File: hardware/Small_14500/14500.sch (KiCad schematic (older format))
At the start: 49 parts, among them J2 Battery, J3 GPIO, J4 USB_B_Micro, J5 Power, J6 LEDs, J7 GPIO, Q1 BSS806N, Q2 BSS806N, Q3 BSS806N, Q4 BSS806N, SW1 Mode, SW2 Power, U1 STM32L072KZUx, U2 AP2210N-3.3TRG1, U3 MCP73831T-2ACI_OT, U4 ESD7002WTT1G

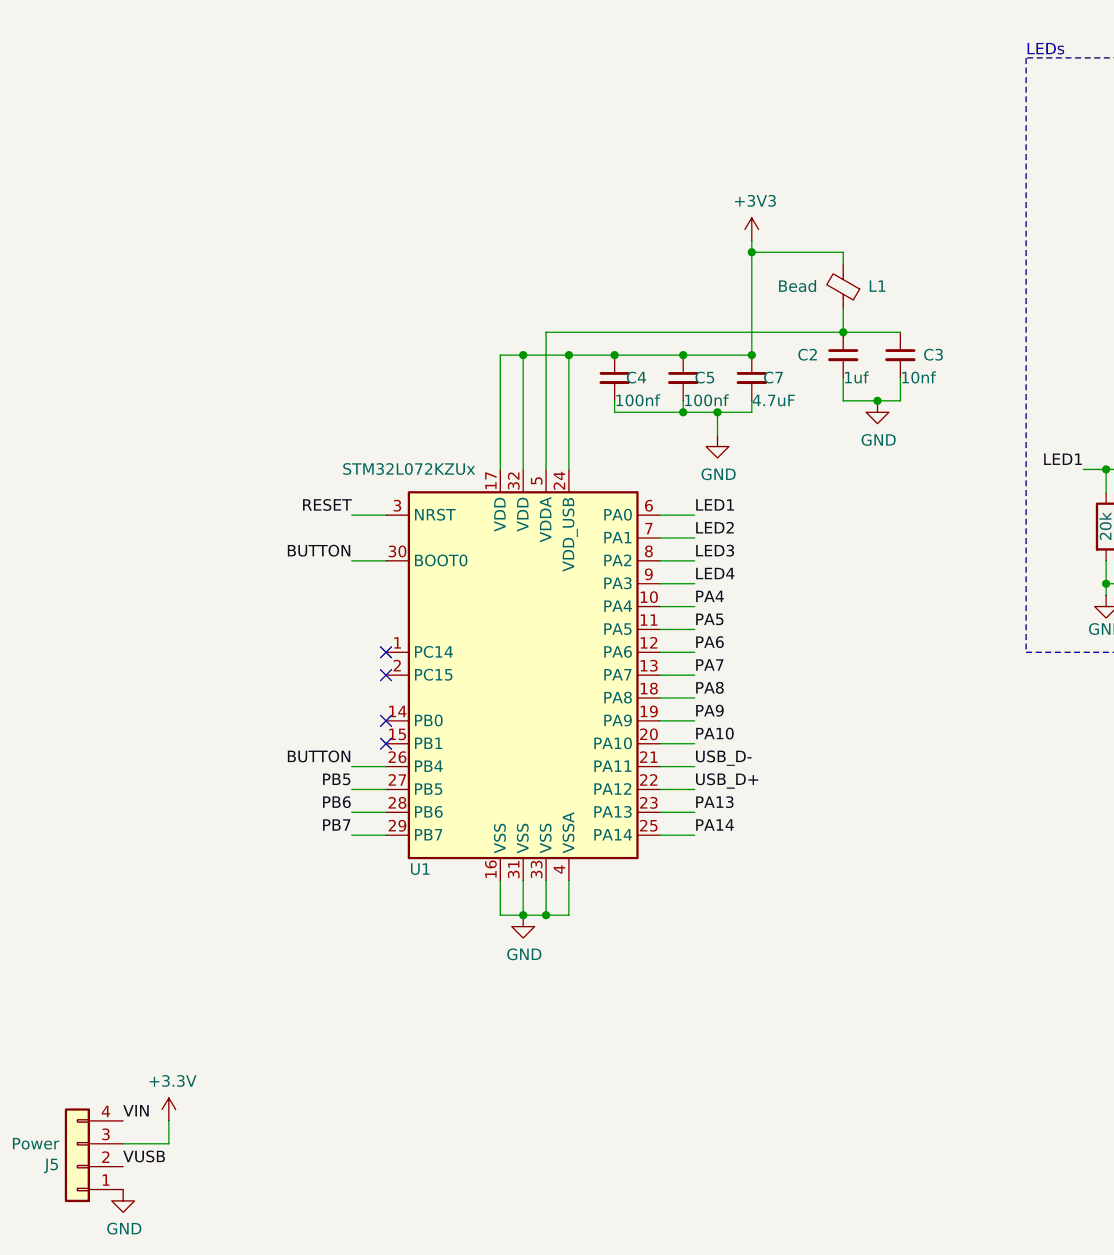
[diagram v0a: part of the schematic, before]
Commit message: Use STM32F412CGUx (Regular & Tiny)
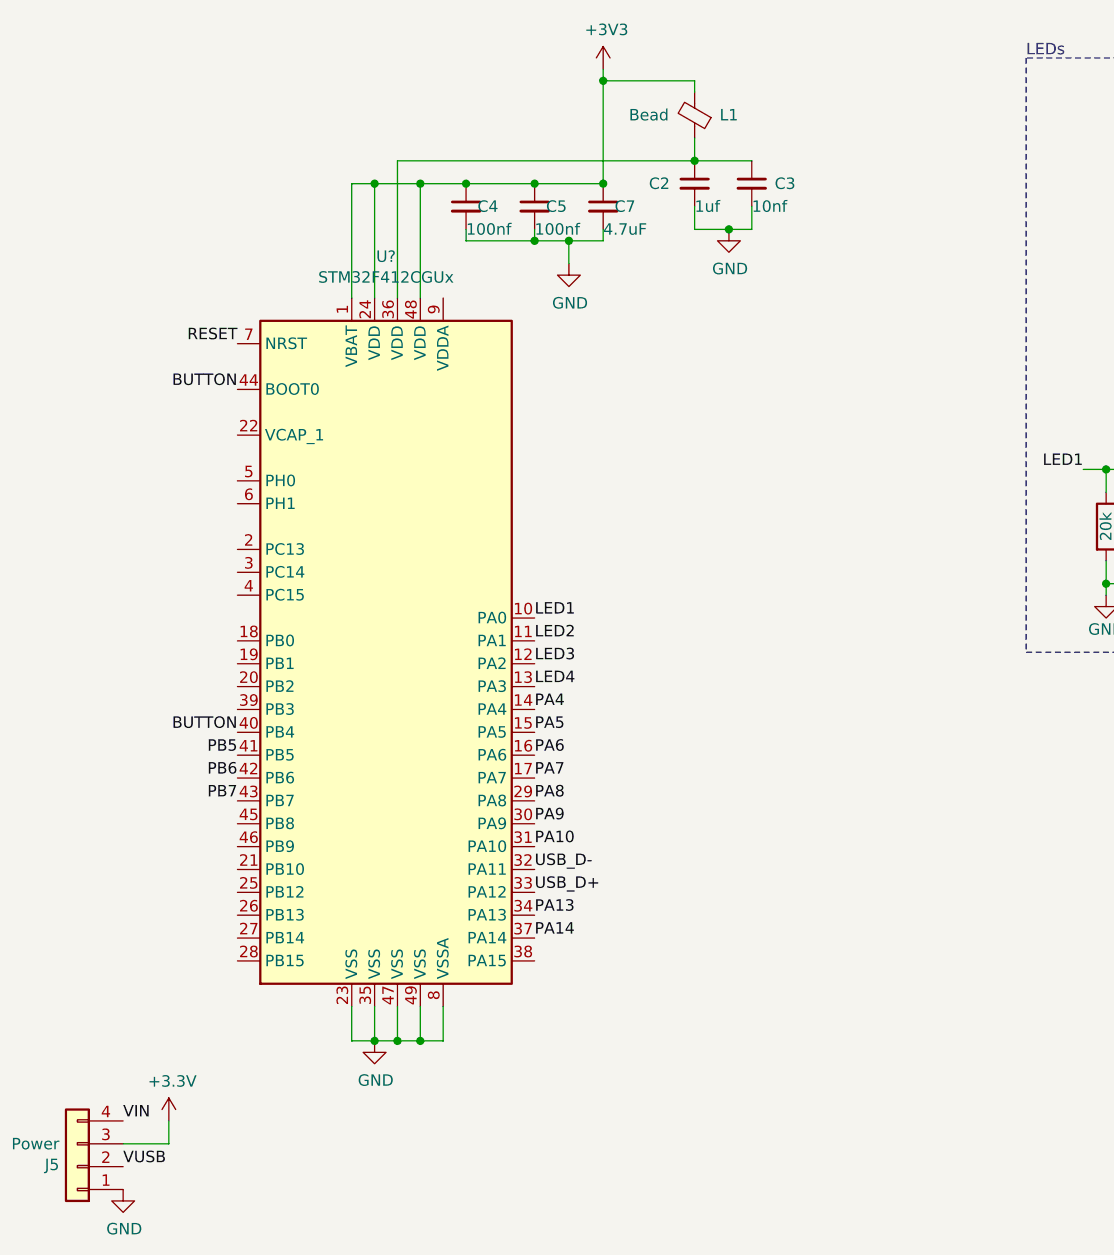
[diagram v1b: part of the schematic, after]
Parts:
- removed U1: STM32L072KZUx, Package_DFN_QFN:QFN-32-1EP_5x5mm_P0.5mm_EP3.45x3.45mm, symbol MCU_ST_STM32L0:STM32L072KZUx
- added U?: STM32F412CGUx, Package_DFN_QFN:QFN-48-1EP_7x7mm_P0.5mm_EP5.6x5.6mm, symbol MCU_ST_STM32F4:STM32F412CGUx
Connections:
- net +3V3: now also U?.1 (VBAT), U?.24 (VDD), U?.48 (VDD)
- net BUTTON: now also U?.40 (PB4), U?.44 (BOOT0)
- net GND: now also U?.23 (VSS), U?.35 (VSS), U?.47 (VSS), U?.49 (VSS), U?.8 (VSSA)
- net LED1: now also U?.10 (PA0)
- net LED2: now also U?.11 (PA1)
- net LED3: now also U?.12 (PA2)
- net LED4: now also U?.13 (PA3)
- net PA10: now also U?.31 (PA10)
- net PA13: now also U?.34 (PA13)
- net PA14: now also U?.37 (PA14)
- net PA4: now also U?.14 (PA4)
- net PA5: now also U?.15 (PA5)
- net PA6: now also U?.16 (PA6)
- net PA7: now also U?.17 (PA7)
- net PA8: now also U?.29 (PA8)
- net PA9: now also U?.30 (PA9)
- net PB5: now also U?.41 (PB5)
- net PB6: now also U?.42 (PB6)
- net PB7: now also U?.43 (PB7)
- net RESET: now also U?.7 (NRST)
- net USB_D+: now also U?.33 (PA12)
- net USB_D-: now also U?.32 (PA11)
- net at C2.1, C3.1, L1.1: now also U?.36 (VDD)
- no-connect marks 5 -> 1
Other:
- moved on the sheet: C2, C3, C4, C5, C7, L1

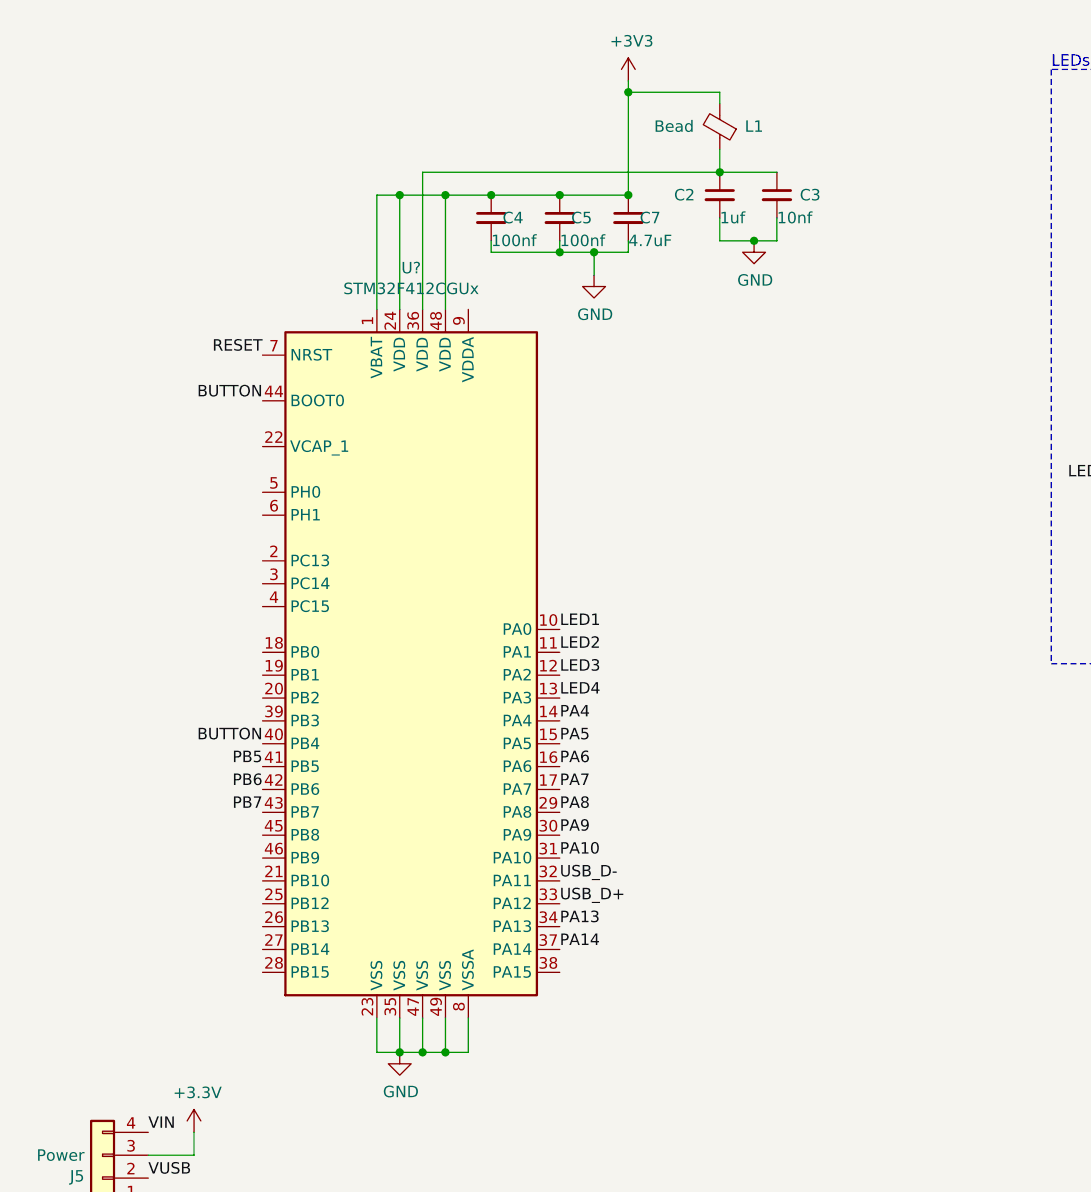
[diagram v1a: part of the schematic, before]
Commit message: Finish updating Small board with STM32F4
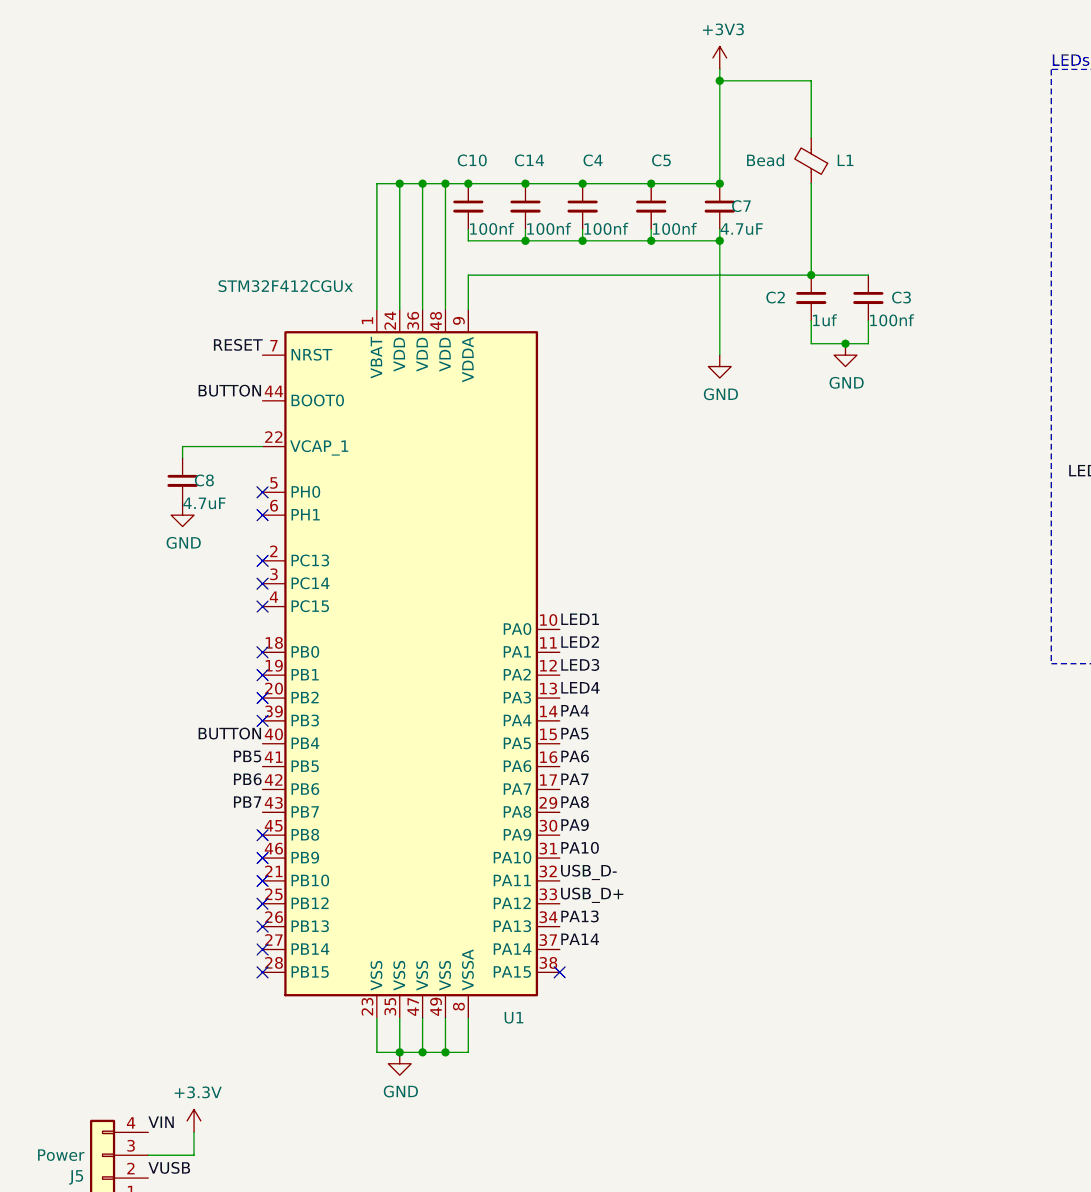
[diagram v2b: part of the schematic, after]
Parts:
- added C10, C14: 100nf, Capacitor_SMD:C_0603_1608Metric, symbol Device:C_Small
- added C8: 4.7uF, Capacitor_SMD:C_0603_1608Metric, symbol Device:C_Small
- C3: value 10nf -> 100nf; MFN CC0603KRX7R9BB103 -> 06035C104K4T2A; MPN Yageo -> (none)
- gave numbers to parts that had none: 1
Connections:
- net +3V3: now also U1.36 (VDD), C10.1, C14.1
- net GND: now also C10.2, C14.2, C8.2
- net at C2.1, C3.1, L1.1: now also U1.9 (VDDA); no longer U1.36 (VDD)
- net at U1.22 (VCAP_1): now also C8.1
- no-connect marks 1 -> 18
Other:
- moved on the sheet: C2, C3, C4, C5, C7, L1

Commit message: Update gerbers
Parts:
- removed J5: Power, Connector_PinHeader_2.54mm:PinHeader_1x04_P2.54mm_Vertical, symbol Connector_Generic:Conn_01x04
- J7: footprint Connector_PinHeader_2.54mm:PinHeader_1x08_P2.54mm_Vertical -> Connector_PinHeader_2.54mm:PinHeader_1x12_P2.54mm_Vertical; symbol Connector_Generic:Conn_01x08 -> Connector_Generic:Conn_01x12
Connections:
- net +3V3: now also J7.11 (Pin_11)
- net GND: now also J7.9 (Pin_9)
- net VIN: now also J7.12 (Pin_12)
- net VUSB: now also J7.10 (Pin_10)
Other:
- moved on the sheet: J3
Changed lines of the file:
@@
 Text Label 3050 1950 2    50   ~ 0
 RESET
-Text Label 1000 5450 0    50   ~ 0
+Text Label 1000 5650 0    50   ~ 0
 PB5
-Text Label 1000 5350 0    50   ~ 0
+Text Label 1000 5550 0    50   ~ 0
 PB6
-Text Label 1000 5850 0    50   ~ 0
+Text Label 1000 6050 0    50   ~ 0
 PA9
-Text Label 1000 5750 0    50   ~ 0
+Text Label 1000 5950 0    50   ~ 0
 PA10
 Wire Wire Line
-	2750 5450 2550 5450
-Wire Wire Line
-	2750 5350 2750 5450
+	1200 5050 1000 5050
+Wire Wire Line
+	1200 4950 1200 5050
 $Comp
 L power:+3.3V #PWR0130
 U 1 1 5C2D9A3C
-P 2750 5350
-F 0 "#PWR0130" H 2750 5200 50  0001 C CNN
-F 1 "+3.3V" H 2765 5523 50  0000 C CNN
-F 2 "" H 2750 5350 50  0001 C CNN
-F 3 "" H 2750 5350 50  0001 C CNN
-	1    2750 5350
-	1    0    0    -1
-$EndComp
-$Comp
-L power:GND #PWR0129
-U 1 1 5C2D8F0C
-P 2550 5650
-F 0 "#PWR0129" H 2550 5400 50  0001 C CNN
-F 1 "GND" H 2555 5477 50  0000 C CNN
-F 2 "" H 2550 5650 50  0001 C CNN
-F 3 "" H 2550 5650 50  0001 C CNN
-	1    2550 5650
-	1    0    0    -1
-$EndComp
-$Comp
-L Connector_Generic:Conn_01x04 J?
-U 1 1 5C2B93C1
-P 2350 5550
-AR Path="/5BD64BD8/5C2B93C1" Ref="J?"  Part="1"
-AR Path="/5C2B93C1" Ref="J5"  Part="1"
-F 0 "J5" H 2429 5542 50  0000 L CNN
-F 1 "Power" H 2429 5451 50  0000 L CNN
-F 2 "Connector_PinHeader_2.54mm:PinHeader_1x04_P2.54mm_Vertical" H 2350 5550 50  0001 C CNN
-F 3 "~" H 2350 5550 50  0001 C CNN
-	1    2350 5550
-	-1   0    0    1
-$EndComp
-Text Label 1000 5250 0    50   ~ 0
+P 1200 4950
+F 0 "#PWR0130" H 1200 4800 50  0001 C CNN
+F 1 "+3.3V" H 1215 5123 50  0000 C CNN
+F 2 "" H 1200 4950 50  0001 C CNN
+F 3 "" H 1200 4950 50  0001 C CNN
+	1    1200 4950
+	1    0    0    -1
+$EndComp
+Text Label 1000 5450 0    50   ~ 0
 PB7
-Text Label 1750 5700 0    50   ~ 0
+Text Label 2000 5650 0    50   ~ 0
 PA8
-Text Label 1750 5600 0    50   ~ 0
+Text Label 2000 5550 0    50   ~ 0
 PA7
-Text Label 1750 5500 0    50   ~ 0
+Text Label 2000 5450 0    50   ~ 0
 PA6
-Text Label 1750 5400 0    50   ~ 0
+Text Label 2000 5350 0    50   ~ 0
 PA5
-Text Label 1750 5300 0    50   ~ 0
+Text Label 2000 5250 0    50   ~ 0
 PA4
 Wire Notes Line
@@
 	1    0    0    -1
 $EndComp
-Text Label 2550 5550 0    50   ~ 0
+Text Label 1000 5150 0    50   ~ 0
 VUSB
 $Comp
@@
 Wire Notes Line
 	10600 4600 7500 4600
-Text Label 1000 5650 0    50   ~ 0
+Text Label 1000 5850 0    50   ~ 0
 PA13
-Text Label 1000 5550 0    50   ~ 0
+Text Label 1000 5750 0    50   ~ 0
 PA14
-Text Label 1000 5150 0    50   ~ 0
+Text Label 1000 5350 0    50   ~ 0
 RESET
 $Comp
 L Connector_Generic:Conn_01x05 J?
 U 1 1 5C29837D
-P 1550 5500
+P 1800 5450
 AR Path="/5BD64BD8/5C29837D" Ref="J?"  Part="1"
 AR Path="/5C29837D" Ref="J3"  Part="1"
-F 0 "J3" H 1629 5492 50  0000 L CNN
-F 1 "GPIO" H 1629 5401 50  0000 L CNN
-F 2 "Connector_PinHeader_2.54mm:PinHeader_1x05_P2.54mm_Vertical" H 1550 5500 50  0001 C CNN
-F 3 "~" H 1550 5500 50  0001 C CNN
-	1    1550 5500
+F 0 "J3" H 1879 5442 50  0000 L CNN
+F 1 "GPIO" H 1879 5351 50  0000 L CNN
+F 2 "Connector_PinHeader_2.54mm:PinHeader_1x05_P2.54mm_Vertical" H 1800 5450 50  0001 C CNN
+F 3 "~" H 1800 5450 50  0001 C CNN
+	1    1800 5450
 	-1   0    0    -1
 $EndComp
 $Comp
-L Connector_Generic:Conn_01x08 J?
+L Connector_Generic:Conn_01x12 J?
 U 1 1 5C3E2B10
 P 800 5550
@@
 F 0 "J7" H 879 5542 50  0000 L CNN
 F 1 "GPIO" H 879 5451 50  0000 L CNN
-F 2 "Connector_PinHeader_2.54mm:PinHeader_1x08_P2.54mm_Vertical" H 800 5550 50  0001 C CNN
+F 2 "Connector_PinHeader_2.54mm:PinHeader_1x12_P2.54mm_Vertical" H 800 5550 50  0001 C CNN
 F 3 "~" H 800 5550 50  0001 C CNN
 	1    800  5550
@@
 	1    0    0    -1
 $EndComp
-Text Label 2550 5350 0    50   ~ 0
+Text Label 1000 4950 0    50   ~ 0
 VIN
 $Comp
@@
 	5050 1950 5050 1450
 Connection ~ 5050 1450
+$Comp
+L power:GND #PWR?
+U 1 1 5E3CF092
+P 1350 5350
+F 0 "#PWR?" H 1350 5100 50  0001 C CNN
+F 1 "GND" H 1355 5177 50  0000 C CNN
+F 2 "" H 1350 5350 50  0001 C CNN
+F 3 "" H 1350 5350 50  0001 C CNN
+	1    1350 5350
+	1    0    0    -1
+$EndComp
+Wire Wire Line
+	1350 5350 1350 5250
+Wire Wire Line
+	1350 5250 1000 5250
 $EndSCHEMATC

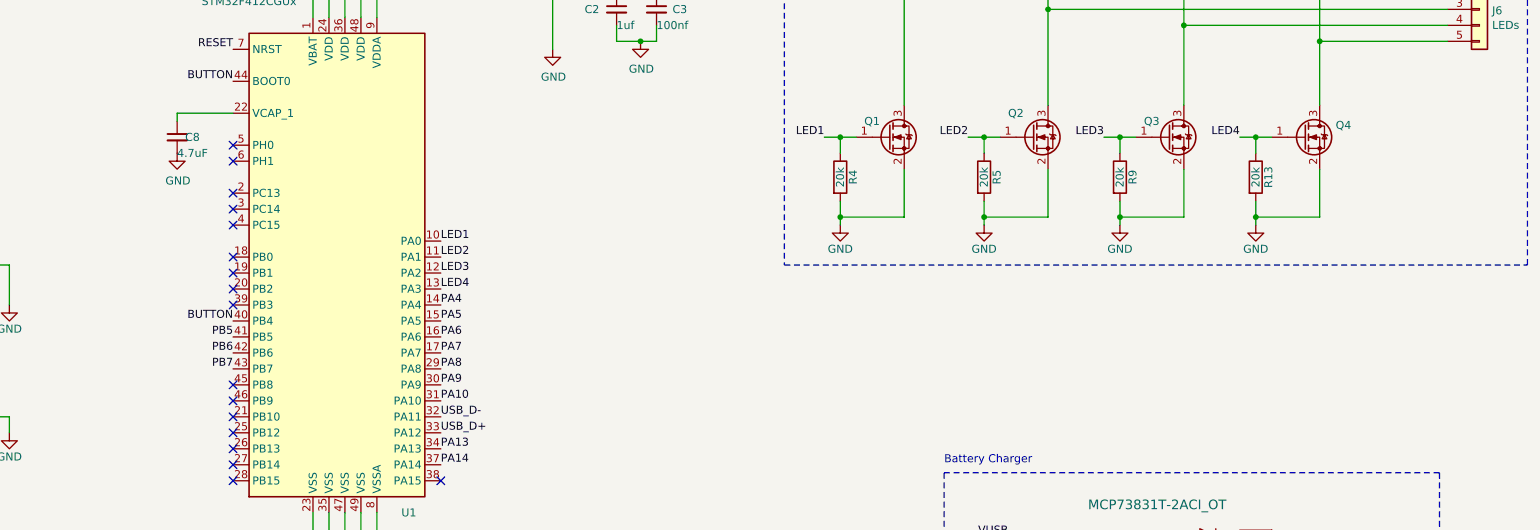
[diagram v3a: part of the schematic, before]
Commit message: Add HSE crystal
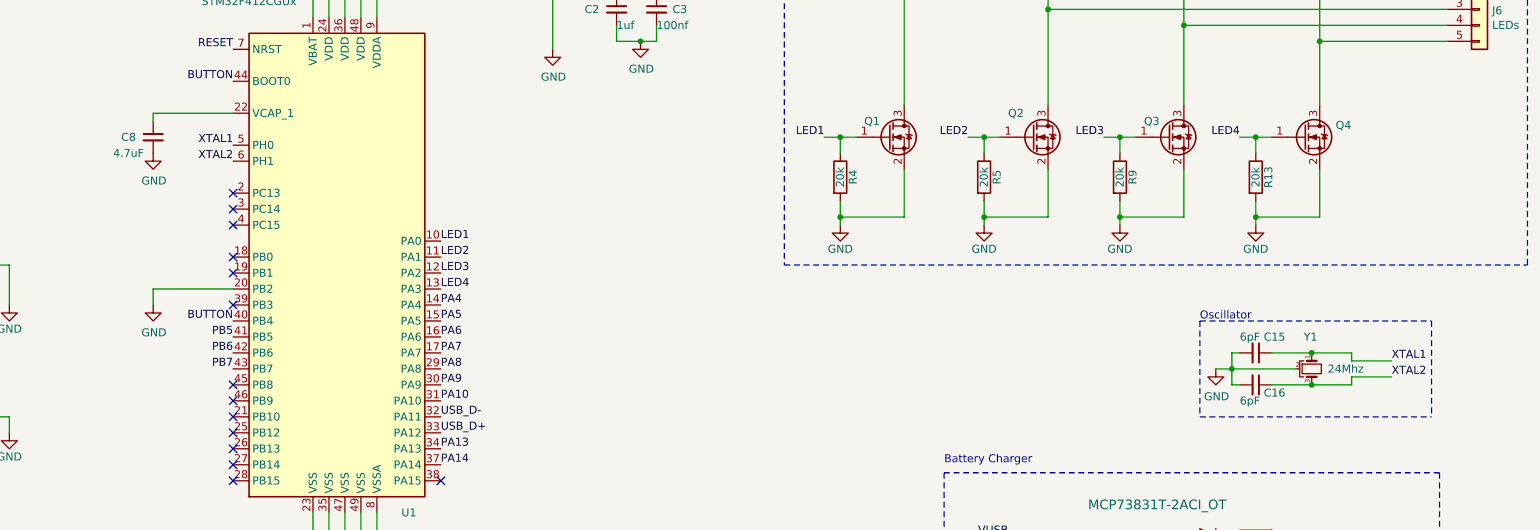
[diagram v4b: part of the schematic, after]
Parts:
- added C15, C16: 6pF, Capacitor_SMD:C_0603_1608Metric, symbol Device:C_Small
- added Y1: 24Mhz, Crystal:Crystal_SMD_2016-4Pin_2.0x1.6mm, symbol Device:Crystal_GND2_Small
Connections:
- net GND: now also U1.20 (PB2), C15.2, C16.2, Y1.2
- net XTAL1: now reaches U1.5 (PH0)
- net XTAL1: now also C15.1, Y1.1
- net XTAL2: now reaches U1.6 (PH1)
- net XTAL2: now also C16.1, Y1.3
- no-connect marks 18 -> 15
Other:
- note added: "Oscillator"
- moved on the sheet: C8
